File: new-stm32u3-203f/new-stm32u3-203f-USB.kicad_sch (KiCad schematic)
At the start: 10 parts, among them J3 12401826E412A, U3 TCPP01-M12

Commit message: added reset button. asigned footprints.
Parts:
- C19, C20: footprint (none) -> Capacitor_SMD:C_0603_1608Metric
- CR1: footprint SOT23-6L_STM -> footprints_usbLC6:SOT23-6L_STM
- CR2: footprint QFN1610_STM -> footprints_esda25:QFN1610_STM
- CR3: footprint SOD-523_STM -> footprints_BAT54:SOD-523_STM
- J3: footprint 12401826_AMP -> footprints_USB_CON:12401826_AMP
- MOSFET1: footprint POWERFLAT-3p3X3p3_STM -> footprints_stl11n3:POWERFLAT-3p3X3p3_STM
- R3, R4: footprint (none) -> Resistor_SMD:R_0603_1608Metric
- U3: footprint QFN12_TCPP01-M12_STM -> Package_DFN_QFN:QFN-12-1EP_3x3mm_P0.5mm_EP1.45x1.45mm
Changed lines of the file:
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@@
 			)
 		)
-		(property "Footprint" ""
+		(property "Footprint" "Resistor_SMD:R_0603_1608Metric"
 			(at 160.02 75.438 90)
 			(effects
@@
 			)
 		)
-		(property "Footprint" "SOT23-6L_STM"
+		(property "Footprint" "footprints_usbLC6:SOT23-6L_STM"
 			(at 86.36 127 0)
 			(effects
@@
 			)
 		)
-		(property "Footprint" "QFN1610_STM"
+		(property "Footprint" "footprints_esda25:QFN1610_STM"
 			(at 170.18 87.63 0)
 			(effects
@@
 			)
 		)
-		(property "Footprint" "SOD-523_STM"
+		(property "Footprint" "footprints_BAT54:SOD-523_STM"
 			(at 240.03 68.58 0)
 			(effects
@@
 			)
 		)
-		(property "Footprint" ""
+		(property "Footprint" "Capacitor_SMD:C_0603_1608Metric"
 			(at 233.9848 59.69 0)
 			(effects
@@
 			)
 		)
-		(property "Footprint" "POWERFLAT-3p3X3p3_STM"
+		(property "Footprint" "footprints_stl11n3:POWERFLAT-3p3X3p3_STM"
 			(at 69.85 54.61 0)
 			(effects
@@
 			)
 		)
-		(property "Footprint" ""
+		(property "Footprint" "Resistor_SMD:R_0603_1608Metric"
 			(at 148.59 70.358 90)
 			(effects
@@
 			)
 		)
-		(property "Footprint" "12401826_AMP"
+		(property "Footprint" "footprints_USB_CON:12401826_AMP"
 			(at 170.18 107.95 0)
 			(effects
@@
 			)
 		)
-		(property "Footprint" ""
+		(property "Footprint" "Capacitor_SMD:C_0603_1608Metric"
 			(at 107.95 98.0948 0)
 			(effects
@@
 			)
 		)
-		(property "Footprint" "QFN12_TCPP01-M12_STM"
+		(property "Footprint" "Package_DFN_QFN:QFN-12-1EP_3x3mm_P0.5mm_EP1.45x1.45mm"
 			(at 166.37 55.88 0)
 			(effects

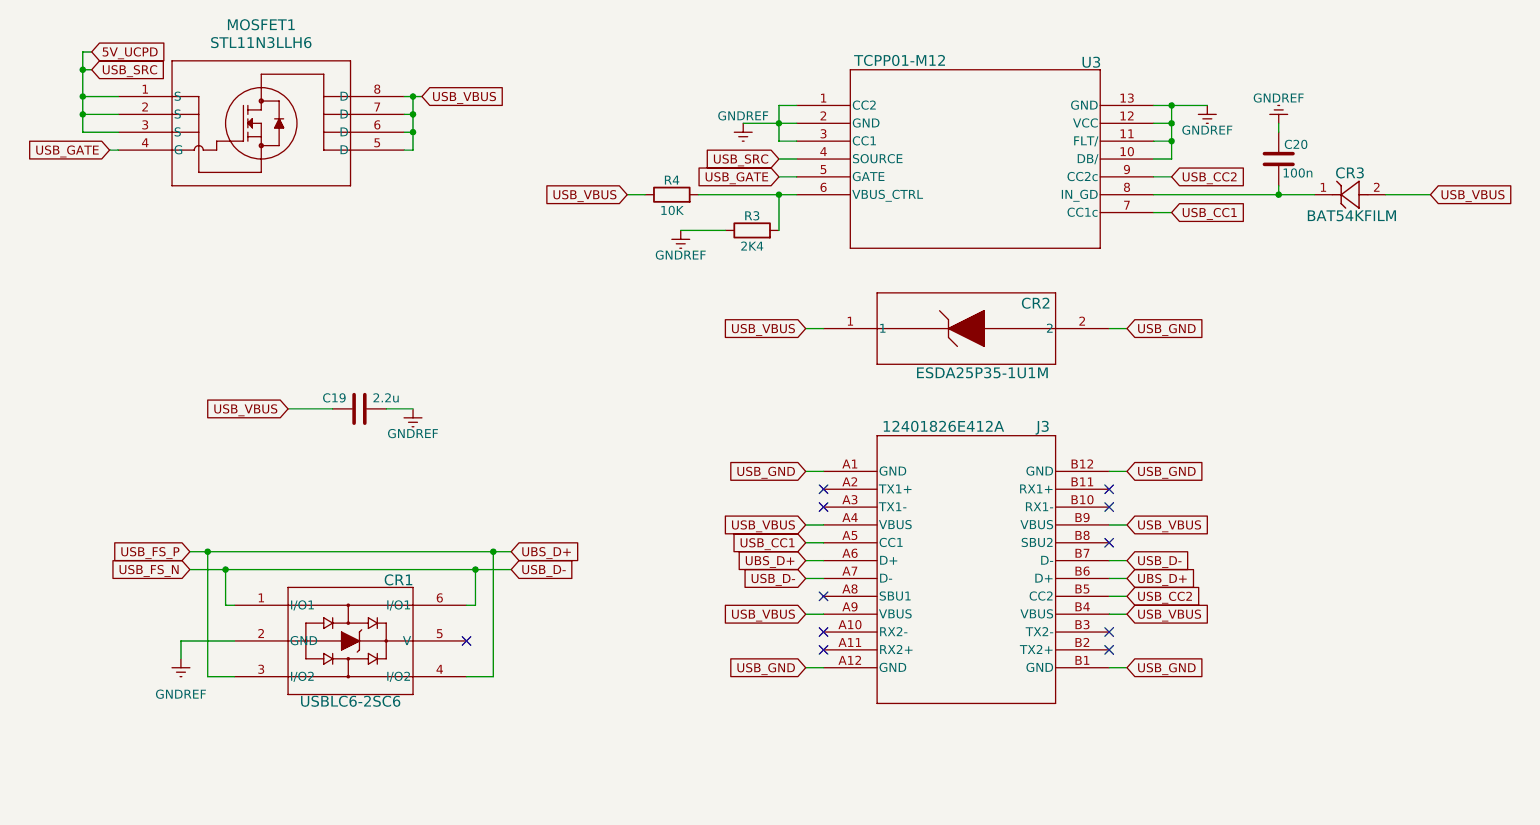
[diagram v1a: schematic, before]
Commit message: moved over to just using direct usb 2.0, made progress on pcb layout
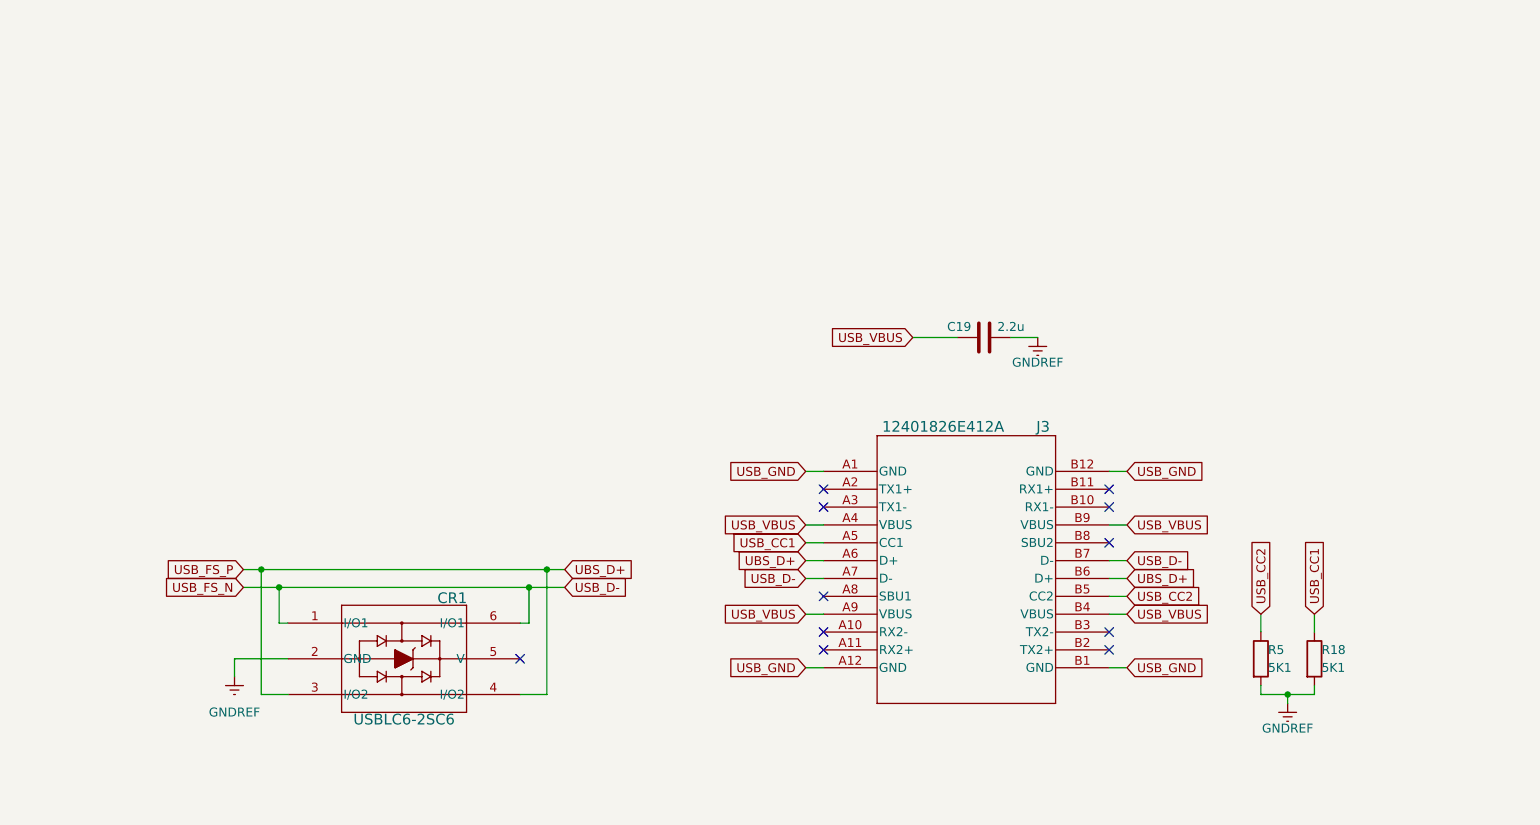
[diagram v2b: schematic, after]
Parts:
- removed C20: 100n, Capacitor_SMD:C_0603_1608Metric, symbol Device:C
- removed CR2: ESDA25P35-1U1M, footprints_esda25:QFN1610_STM, symbol 2026-01-24_13-06-26:ESDA25P35-1U1M
- removed CR3: BAT54KFILM, footprints_BAT54:SOD-523_STM, symbol 2026-01-26_03-59-16:BAT54KFILM
- removed MOSFET1: STL11N3LLH6, footprints_stl11n3:POWERFLAT-3p3X3p3_STM, symbol 2026-01-26_04-02-48:STL11N3LLH6
- removed R3: 2K4, Resistor_SMD:R_0603_1608Metric, symbol Device:R
- removed R4: 10K, Resistor_SMD:R_0603_1608Metric, symbol Device:R
- removed U3: TCPP01-M12, Package_DFN_QFN:QFN-12-1EP_3x3mm_P0.5mm_EP1.45x1.45mm, symbol 2026-01-26_03-34-42:TCPP01-M12
- added R18, R5: 5K1, Resistor_SMD:R_0603_1608Metric, symbol Device:R
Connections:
- net GNDREF: now also R18.2, R5.2
- net USB_CC1: now also R18.1
- net USB_CC2: now also R5.1
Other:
- moved on the sheet: C19, CR1

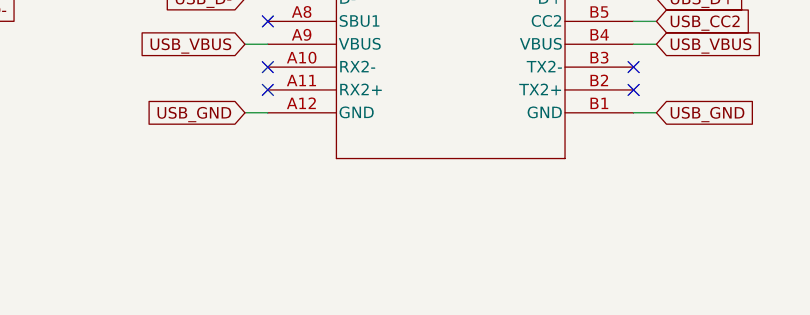
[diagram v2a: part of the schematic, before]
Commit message: restarted routing and started using 6 layers and power planes.
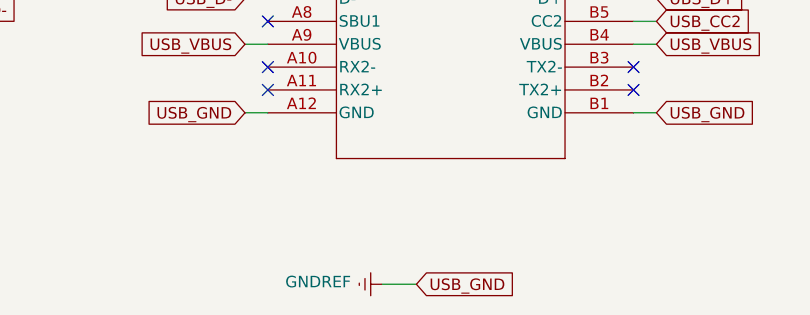
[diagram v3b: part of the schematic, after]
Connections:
- net USB_GND is gone; now on net GNDREF: J3.A1 (GND), J3.A12 (GND), J3.B1 (GND), J3.B12 (GND)
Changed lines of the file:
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@@
+	(wire
+		(pts
+			(xy 182.88 154.94) (xy 186.69 154.94)
+		)
+		(stroke
+			(width 0)
+			(type default)
+		)
+	)
 	(wire
 		(pts
@@
 				)
 				(justify right)
+				(hide yes)
+			)
+		)
+	)
+	(global_label "USB_GND"
+		(shape input)
+		(at 186.69 154.94 0)
+		(fields_autoplaced yes)
+		(effects
+			(font
+				(size 1.27 1.27)
+			)
+			(justify left)
+		)
+		(property "Intersheetrefs" "${INTERSHEET_REFS}"
+			(at 198.3233 154.94 0)
+			(effects
+				(font
+					(size 1.27 1.27)
+				)
+				(justify left)
 				(hide yes)
 			)
@@
 					(unit 1)
 				)
+			)
+		)
+	)
+	(symbol
+		(lib_id "power:GNDREF")
+		(at 182.88 154.94 270)
+		(mirror x)
+		(unit 1)
+		(exclude_from_sim no)
+		(in_bom yes)
+		(on_board yes)
+		(dnp no)
+		(property "Reference" "#PWR066"
+			(at 176.53 154.94 0)
+			(effects
+				(font
+					(size 1.27 1.27)
+				)
+				(hide yes)
+			)
+		)
+		(property "Value" "GNDREF"
+			(at 175.768 154.686 90)
+			(effects
+				(font
+					(size 1.27 1.27)
+				)
+			)
+		)
+		(property "Footprint" ""
+			(at 182.88 154.94 0)
+			(effects
+				(font
+					(size 1.27 1.27)
+				)
+				(hide yes)
+			)
+		)
+		(property "Datasheet" ""
+			(at 182.88 154.94 0)
+			(effects
+				(font
+					(size 1.27 1.27)
+				)
+				(hide yes)
+			)
+		)
+		(property "Description" "Power symbol creates a global label with name \"GNDREF\" , reference supply ground"
+			(at 182.88 154.94 0)
+			(effects
+				(font
+					(size 1.27 1.27)
+				)
+				(hide yes)
+			)
+		)
+		(pin "1"
+		)
+		(instances
+			(project "new-stm32u3-203f"
+				(path "/133609ce-1e1a-4c9a-bce3-37a0219dc965/34bad8bb-28b3-48fe-82c5-aa0a12365f06"
+					(reference "#PWR066")
+					(unit 1)
+				)

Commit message: finished more errors, started adding extra stuff.
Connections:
- net GNDREF: now also J3.C1 (Sheild)
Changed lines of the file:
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@@
+	(wire
+		(pts
+			(xy 190.5 147.32) (xy 190.5 143.51)
+		)
+		(stroke
+			(width 0)
+			(type default)
+		)
+	)
 	(wire
 		(pts
@@
 		(pts
 			(xy 210.82 107.95) (xy 213.36 107.95)
+		)
+		(stroke
+			(width 0)
+			(type default)
+		)
+	)
+	(wire
+		(pts
+			(xy 191.77 147.32) (xy 190.5 147.32)
 		)
 		(stroke
@@
 	(symbol
 		(lib_id "power:GNDREF")
+		(at 191.77 147.32 90)
+		(unit 1)
+		(exclude_from_sim no)
+		(in_bom yes)
+		(on_board yes)
+		(dnp no)
+		(property "Reference" "#PWR070"
+			(at 198.12 147.32 0)
+			(effects
+				(font
+					(size 1.27 1.27)
+				)
+				(hide yes)
+			)
+		)
+		(property "Value" "GNDREF"
+			(at 198.882 147.066 90)
+			(effects
+				(font
+					(size 1.27 1.27)
+				)
+			)
+		)
+		(property "Footprint" ""
+			(at 191.77 147.32 0)
+			(effects
+				(font
+					(size 1.27 1.27)
+				)
+				(hide yes)
+			)
+		)
+		(property "Datasheet" ""
+			(at 191.77 147.32 0)
+			(effects
+				(font
+					(size 1.27 1.27)
+				)
+				(hide yes)
+			)
+		)
+		(property "Description" "Power symbol creates a global label with name \"GNDREF\" , reference supply ground"
+			(at 191.77 147.32 0)
+			(effects
+				(font
+					(size 1.27 1.27)
+				)
+				(hide yes)
+			)
+		)
+		(pin "1"
+		)
+		(instances
+			(project "new-stm32u3-203f"
+				(path "/133609ce-1e1a-4c9a-bce3-37a0219dc965/34bad8bb-28b3-48fe-82c5-aa0a12365f06"
+					(reference "#PWR070")
+					(unit 1)
+				)
+			)
+		)
+	)
+	(symbol
+		(lib_id "power:GNDREF")
 		(at 182.88 154.94 270)
 		(mirror x)
@@
 		(pin "B6"
 		)
+		(pin "C1"
+		)
 		(instances

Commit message: fixed drc and some other things.
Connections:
- net GNDREF: no longer J3.C1 (Sheild)
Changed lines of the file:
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@@
-	(wire
-		(pts
-			(xy 190.5 147.32) (xy 190.5 143.51)
-		)
-		(stroke
-			(width 0)
-			(type default)
-		)
-	)
 	(wire
 		(pts
@@
 		(pts
 			(xy 210.82 107.95) (xy 213.36 107.95)
-		)
-		(stroke
-			(width 0)
-			(type default)
-		)
-	)
-	(wire
-		(pts
-			(xy 191.77 147.32) (xy 190.5 147.32)
 		)
 		(stroke
@@
 					(unit 1)
 				)
-			)
-		)
-	)
-	(symbol
-		(lib_id "power:GNDREF")
-		(at 191.77 147.32 90)
-		(unit 1)
-		(exclude_from_sim no)
-		(in_bom yes)
-		(on_board yes)
-		(dnp no)
-		(property "Reference" "#PWR070"
-			(at 198.12 147.32 0)
-			(effects
-				(font
-					(size 1.27 1.27)
-				)
-				(hide yes)
-			)
-		)
-		(property "Value" "GNDREF"
-			(at 198.882 147.066 90)
-			(effects
-				(font
-					(size 1.27 1.27)
-				)
-			)
-		)
-		(property "Footprint" ""
-			(at 191.77 147.32 0)
-			(effects
-				(font
-					(size 1.27 1.27)
-				)
-				(hide yes)
-			)
-		)
-		(property "Datasheet" ""
-			(at 191.77 147.32 0)
-			(effects
-				(font
-					(size 1.27 1.27)
-				)
-				(hide yes)
-			)
-		)
-		(property "Description" "Power symbol creates a global label with name \"GNDREF\" , reference supply ground"
-			(at 191.77 147.32 0)
-			(effects
-				(font
-					(size 1.27 1.27)
-				)
-				(hide yes)
-			)
-		)
-		(pin "1"
-		)
-		(instances
-			(project "new-stm32u3-203f"
-				(path "/133609ce-1e1a-4c9a-bce3-37a0219dc965/34bad8bb-28b3-48fe-82c5-aa0a12365f06"
-					(reference "#PWR070")
-					(unit 1)
-				)
